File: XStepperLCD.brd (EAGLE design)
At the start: 49.5 x 38.1 mm, 43 parts, among them Q2 16 MHZ, U1 LCD-16X2NOHOLES

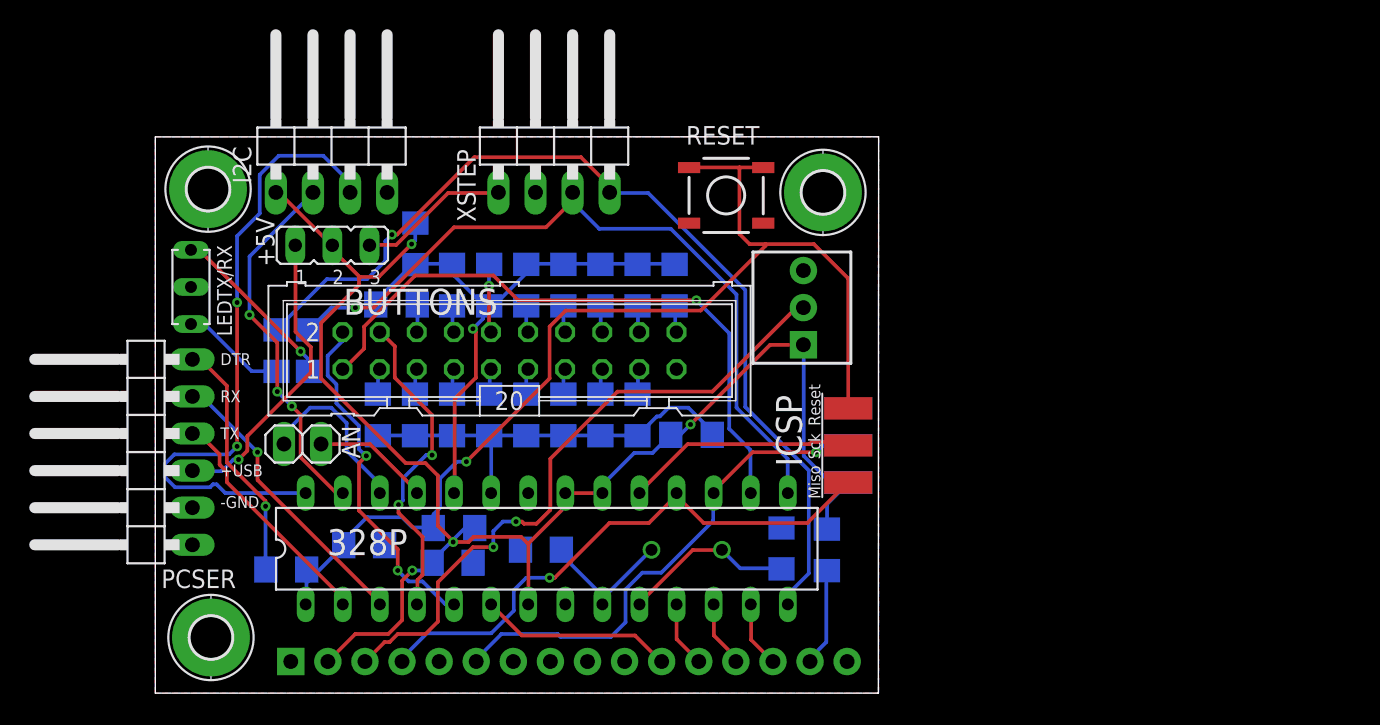
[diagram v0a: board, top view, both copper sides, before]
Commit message: - get button values only from A0
- stop/restart all threads in get values command
- refresh silkscreen in board and design
- set version 0.2 in code
- remove some comments
- add group init for threads
- reformat code
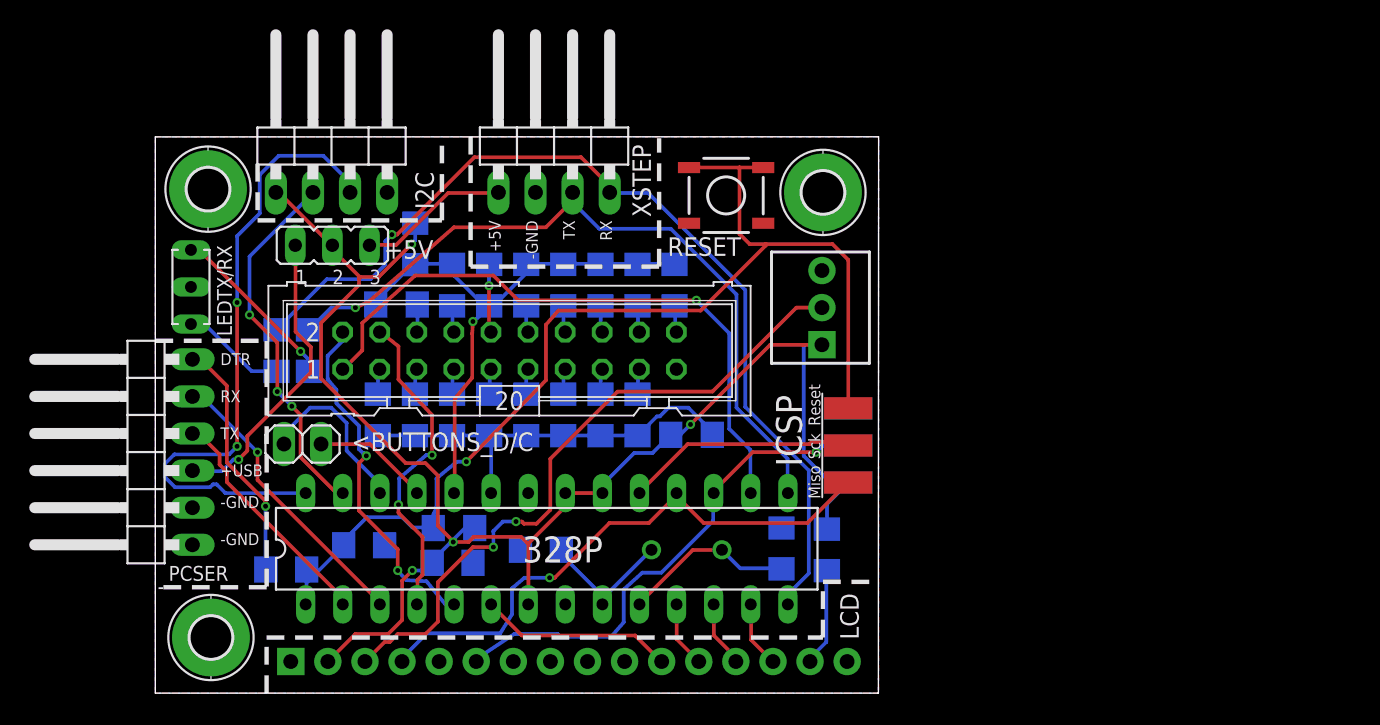
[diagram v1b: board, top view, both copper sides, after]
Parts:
- R2: value 220 -> 0-220R
- moved R1 1.27 mm to (45.3, 26.4)
- renumbered AN to <BUTTONS_D/C
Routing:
- net VCC: track 104.4 -> 106.9 mm
- net N$1: track 44.5 -> 45.7 mm
- net RESET: track 76.1 -> 77.1 mm
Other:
- board text added: "+5V"
- board text added: "680R"
- board text added: "LCD"
- board text added: "XLCD 0.2/092013"
- board text removed: "XSTEP 0.2 / 092013"

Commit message: - bugfic: set all buttons resistor to different values
- fix schema and board
- fix some typos and bugs in readButtons
- add thread to read buttons
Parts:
- R10, R18: value 680 -> 1.8k
- R11, R19: value 680 -> 2.2k
- R12, R20: value 680 -> 2.7k
- R13, R21: value 680 -> 3.3k
- R14, R22: value 680 -> 3.9k
- R15, R23: value 680 -> 4.7k
- R17, R9: value 680 -> 1.2k
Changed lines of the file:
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@@
 <?xml version="1.0" encoding="utf-8"?>
 <!DOCTYPE eagle SYSTEM "eagle.dtd">
-<eagle version="6.5.0">
+<eagle version="6.3">
 <drawing>
 <settings>
@@
 <wire x1="49.53" y1="38.1" x2="0" y2="38.09" width="0" layer="20"/>
 <wire x1="0" y1="38.09" x2="0" y2="0" width="0" layer="20"/>
-<dimension x1="0" y1="48.26" x2="49.53" y2="48.26" x3="24.765" y3="63.5" textsize="1.778" layer="51"/>
-<dimension x1="49.53" y1="48.26" x2="49.53" y2="0" x3="58.42" y3="24.13" textsize="1.778" layer="51"/>
+<dimension x1="0" y1="48.26" x2="49.53" y2="48.26" x3="24.765" y3="63.5" layer="51"/>
+<dimension x1="49.53" y1="48.26" x2="49.53" y2="0" x3="58.42" y3="24.13" layer="51"/>
 <text x="44.28" y="15.525" size="1.778" layer="25" rot="R90">ICSP</text>
 <text x="45.54" y="18.31" size="0.8128" layer="25" rot="R90">Reset</text>
@@
 </element>
 <element name="R8" library="resistor" package="R1206" value="680" x="16.515" y="26.61" smashed="yes" rot="MR0"/>
-<element name="R9" library="resistor" package="R1206" value="680" x="20.32" y="27.94" smashed="yes" rot="MR90"/>
-<element name="R10" library="resistor" package="R1206" value="680" x="22.86" y="27.94" smashed="yes" rot="MR270"/>
-<element name="R11" library="resistor" package="R1206" value="680" x="25.4" y="27.94" smashed="yes" rot="MR90"/>
-<element name="R12" library="resistor" package="R1206" value="680" x="27.94" y="27.94" smashed="yes" rot="MR90"/>
-<element name="R13" library="resistor" package="R1206" value="680" x="30.48" y="27.94" smashed="yes" rot="MR90"/>
-<element name="R14" library="resistor" package="R1206" value="680" x="33.02" y="27.94" smashed="yes" rot="MR90"/>
-<element name="R15" library="resistor" package="R1206" value="680" x="35.56" y="27.94" smashed="yes" rot="MR90"/>
+<element name="R9" library="resistor" package="R1206" value="1.2k" x="20.32" y="27.94" smashed="yes" rot="MR90"/>
+<element name="R10" library="resistor" package="R1206" value="1.8k" x="22.86" y="27.94" smashed="yes" rot="MR270"/>
+<element name="R11" library="resistor" package="R1206" value="2.2k" x="25.4" y="27.94" smashed="yes" rot="MR90"/>
+<element name="R12" library="resistor" package="R1206" value="2.7k" x="27.94" y="27.94" smashed="yes" rot="MR90"/>
+<element name="R13" library="resistor" package="R1206" value="3.3k" x="30.48" y="27.94" smashed="yes" rot="MR90"/>
+<element name="R14" library="resistor" package="R1206" value="3.9k" x="33.02" y="27.94" smashed="yes" rot="MR90"/>
+<element name="R15" library="resistor" package="R1206" value="4.7k" x="35.56" y="27.94" smashed="yes" rot="MR90"/>
 <element name="R16" library="resistor" package="R1206" value="680" x="33.02" y="19.05" smashed="yes" rot="MR270"/>
-<element name="R17" library="resistor" package="R1206" value="680" x="30.48" y="19.05" smashed="yes" rot="MR270"/>
-<element name="R18" library="resistor" package="R1206" value="680" x="27.94" y="19.05" smashed="yes" rot="MR270"/>
-<element name="R19" library="resistor" package="R1206" value="680" x="25.4" y="19.05" smashed="yes" rot="MR270"/>
-<element name="R20" library="resistor" package="R1206" value="680" x="22.86" y="19.05" smashed="yes" rot="MR270"/>
-<element name="R21" library="resistor" package="R1206" value="680" x="20.32" y="19.05" smashed="yes" rot="MR270"/>
-<element name="R22" library="resistor" package="R1206" value="680" x="17.78" y="19.05" smashed="yes" rot="MR270"/>
-<element name="R23" library="resistor" package="R1206" value="680" x="15.24" y="19.05" smashed="yes" rot="MR270"/>
+<element name="R17" library="resistor" package="R1206" value="1.2k" x="30.48" y="19.05" smashed="yes" rot="MR270"/>
+<element name="R18" library="resistor" package="R1206" value="1.8k" x="27.94" y="19.05" smashed="yes" rot="MR270"/>
+<element name="R19" library="resistor" package="R1206" value="2.2k" x="25.4" y="19.05" smashed="yes" rot="MR270"/>
+<element name="R20" library="resistor" package="R1206" value="2.7k" x="22.86" y="19.05" smashed="yes" rot="MR270"/>
+<element name="R21" library="resistor" package="R1206" value="3.3k" x="20.32" y="19.05" smashed="yes" rot="MR270"/>
+<element name="R22" library="resistor" package="R1206" value="3.9k" x="17.78" y="19.05" smashed="yes" rot="MR270"/>
+<element name="R23" library="resistor" package="R1206" value="4.7k" x="15.24" y="19.05" smashed="yes" rot="MR270"/>
 <element name="&lt;BUTTONS_D/C" library="pinhead" package="1X02" value="Analog" x="10.08" y="17.06" smashed="yes" rot="R180">
 <attribute name="NAME" x="13.4288" y="16.5788" size="1.27" layer="25" ratio="10"/>
@@
 </signal>
 </signals>
-<errors>
-</errors>
 </board>
 </drawing>

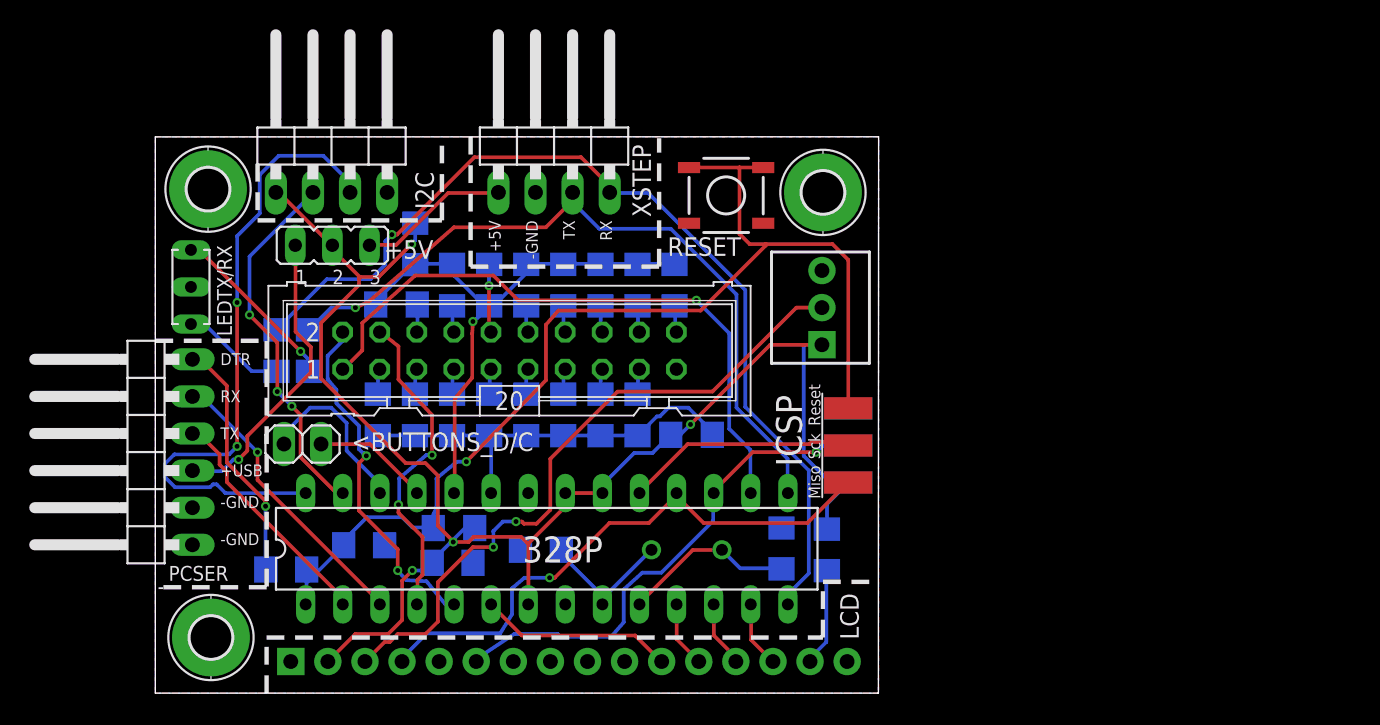
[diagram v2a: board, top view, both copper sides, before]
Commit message: - replace some TH parts with SMD and bugfixes
- remove reset button
- remove power pin and choose only power from xstepper
- add RJ45 plugin for connect XStepper
- change all button resistors to 680r and connect serial
- remove LED from serial line and put a new one to A7
- add some text to I2C
- change Atmega328 to SMD Version
- change Quartz to SMD ceramic resonator (16MHz)
- replace ICSP to normal 2x3 pin header
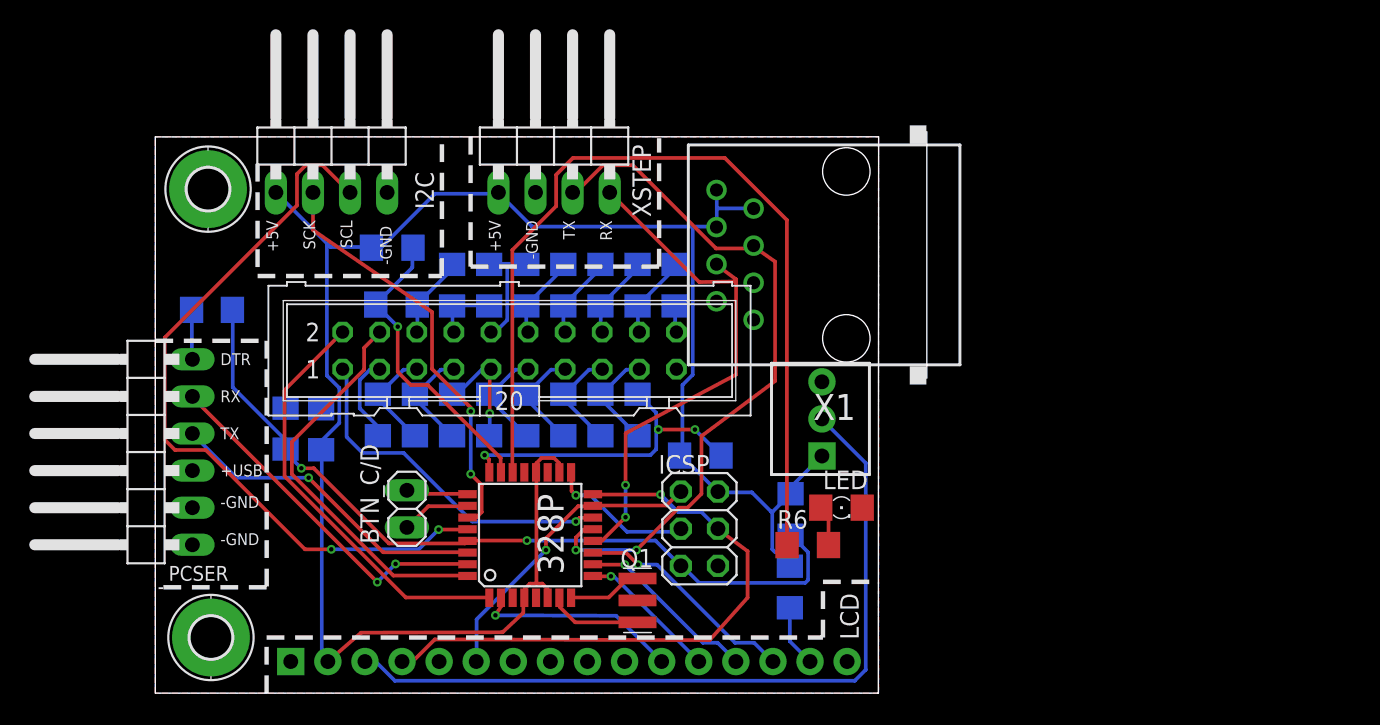
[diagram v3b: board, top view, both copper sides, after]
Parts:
- removed +5V: USB_VCC, jumper:JP2
- removed <BUTTONS_D/C: Analog, pinhead:1X02
- removed C14, C15: 18pF, resistor:C1206
- removed H6: MOUNT-PAD-ROUND2.8, holes:2,8-PAD
- removed LEDTX/RX: (no value), led:DUOLED2X5
- removed Q2: 16 MHZ, crystal:HC49/S
- removed R7: 110, resistor:R1206
- removed RESET: RESET, SparkFun:TACTILE_SWITCH_SMD
- added BTN_C/D: Analog, pinhead:1X02
- added LED: (no value), led:1206
- added Q1: (no value), murata-filter:CSTCR6M
- added X1: RJ45-6L-B, con-tycoelectronics:RJ45-NO-SHIELD
- 328P: device Bibsatmel:DIL28-3 -> atmel:TQFP32-08
- ICSP: value ICSP -> (none); device avr-7:6PAD_ISP -> pinhead:2X03
- R10, R18: value 1.8k -> 680
- R11, R19: value 2.2k -> 680
- R12, R20: value 2.7k -> 680
- R13, R21: value 3.3k -> 680
- R14, R22: value 3.9k -> 680
- R15, R23: value 4.7k -> 680
- R17, R9: value 1.2k -> 680
- R6: value 110 -> 160R
- moved R6 38.7 mm to (44.7, 10.1), flipped to the top, turned to 0 degrees
- moved R3 23.1 mm to (43.5, 12.2), turned to 90 degrees
- moved C1 18.5 mm to (3.88, 26.2)
- moved C12 12.8 mm to (11.4, 18.1), turned to 270 degrees
- moved ICSP 11.7 mm to (37.3, 11.3), turned to 270 degrees
- moved C13 9.62 mm to (8.92, 18.1), turned to 270 degrees
- moved R1 7.62 mm to (45.3, 18.8)
- moved R2 3.59 mm to (43.5, 7.27)
- moved R5 1.60 mm to (16.2, 30.5), turned to 0 degrees
- moved R4 1.54 mm to (37.3, 16.3)
- moved 328P 1.47 mm to (25.7, 10.8), turned to 90 degrees
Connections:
- removed net N$12 (its old number): BUTTONS.12, R11.1
- removed net N$16: BUTTONS.7, R21.1
- removed net N$17: BUTTONS.9, R20.1
- removed net N$18: BUTTONS.11, R19.1
- removed net N$19: BUTTONS.18, R14.1
- removed net N$21: LEDTX/RX.AG, R6.2
- removed net N$22: LEDTX/RX.AR, R7.1
- removed net N$33: 328P.9, C15.1, Q2.1
- removed net USB_5V: +5V.1, PCSER.3
- removed net XSTEP_5V: +5V.3, XSTEP.1
- new net N$23: BUTTONS.17, R16.2, R17.1
- new net N$24: BUTTONS.15, R17.2, R18.1
- new net N$25: BUTTONS.13, R18.2, R19.1
- new net N$26: BUTTONS.11, R19.2, R20.1
- new net N$27: BUTTONS.9, R20.2, R21.1
- new net N$28: BUTTONS.7, R21.2, R22.1
- new net N$29: BUTTONS.5, R22.2, R23.1
- new net N$3: 328P.7, Q1.1
- net BUTTONS_A: now also R5.1, R8.2; no longer R16.2, R17.2, R18.2, R19.2, R20.2, R21.2, R22.2, R23.2, R4.1
- net BUTTONS_B: now also R16.1, R4.1; no longer R10.2, R11.2, R12.2, R13.2, R14.2, R15.2, R5.1, R8.2, R9.2
- net BUTTONS_C: now also BTN_C/D.1; no longer <BUTTONS_D/C.1
- net BUTTONS_D: now also BTN_C/D.2; no longer <BUTTONS_D/C.2
- net D4: now also 328P.2; no longer 328P.6
- net D5: now also 328P.9; no longer 328P.11
- net D6: now also 328P.10; no longer 328P.12
- net D7: now also 328P.11; no longer 328P.13
- net ENABLE/MOSI: now also 328P.15, ICSP.1; no longer 328P.17, ICSP.MOSI
- net GND: now also 328P.21, 328P.3, 328P.5, ICSP.6, LED.C, Q1.2, X1.1, X1.2, X1.3; no longer 328P.22, 328P.8, C14.2, C15.2, H6.B2,8, ICSP.GND, LEDTX/RX.K, RESET.1, RESET.2
- net N$10: now also BUTTONS.18, R14.1, R15.2; no longer BUTTONS.5, R22.1
- net N$11: now also BUTTONS.14, R12.1, R13.2; no longer BUTTONS.10, R10.1
- net N$13: now also LED.A, R6.2; no longer BUTTONS.14, R12.1
- net N$15: now also 328P.22, R6.1; no longer BUTTONS.16, R13.1
- net N$34: now also 328P.8, Q1.3; no longer 328P.10, C14.1, Q2.2
- net N$4: now also BUTTONS.3, R23.2; no longer BUTTONS.13, R18.1
- net N$5: now also BUTTONS.6, R8.1, R9.2; no longer BUTTONS.15, R17.1
- net N$6: now also BUTTONS.8, R10.2, R9.1; no longer BUTTONS.17, R16.1
- net N$7: now also BUTTONS.10, R10.1, R11.2; no longer BUTTONS.6, R8.1
- net N$8: now also BUTTONS.12, R11.1, R12.2; no longer BUTTONS.8, R9.1
- net N$9: now also BUTTONS.16, R13.1, R14.2; no longer BUTTONS.3, R23.1
- net POT_A: now also 328P.32; no longer 328P.4
- net POT_B: now also 328P.1; no longer 328P.5
- net POT_SELECT: now also 328P.14; no longer 328P.16
- net RESET: now also 328P.29, ICSP.5; no longer 328P.1, ICSP.RST, RESET.3, RESET.4
- net RS/MISO: now also 328P.16, ICSP.4; no longer 328P.18, ICSP.MISO
- net RX: now also 328P.12, X1.4; no longer 328P.14, R6.1
- net SCK: now also 328P.17, ICSP.3; no longer 328P.19, ICSP.SCK
- net TX: now also 328P.13, X1.5; no longer 328P.15, R7.2
- net USB_RXD: now also 328P.31; no longer 328P.3
- net USB_TXD: now also 328P.30; no longer 328P.2
- net VCC: now also 328P.18, 328P.4, 328P.6, ICSP.2, X1.6, X1.7, X1.8, XSTEP.1; no longer +5V.2, 328P.21, 328P.7, ICSP.VCC
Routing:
- net N$15: track 1.84 -> 61.9 mm
- net RX: track 65.9 -> 36.7 mm, vias 1 -> 2
- net VCC: track 106.9 -> 132.2 mm, vias 4 -> 0
- net RESET: track 77.1 -> 54.5 mm, vias 1 -> 2
- net USB_5V: track 20.7 -> 0.00 mm, vias 1 -> 0
- net POT_SELECT: track 43.4 -> 24.1 mm
- net BUTTONS_B: track 39.7 -> 22.7 mm, vias 1 -> 3
- net N$14: track 16.8 -> 3.40 mm, vias 1 -> 0
- net ENABLE/MOSI: track 34.2 -> 21.0 mm
- net N$22: track 12.0 -> 0.00 mm, vias 1 -> 0
- net D7: track 4.55 -> 15.4 mm, vias 0 -> 1
- net XSTEP_5V: track 10.3 -> 0.00 mm
- net N$33: track 10.0 -> 0.00 mm
- net BUTTONS_A: track 28.7 -> 20.7 mm, vias 0 -> 1
- net D6: track 4.54 -> 12.6 mm, vias 0 -> 1
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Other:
- board text added: "SCK"
- board text added: "SCL"
- board text added: "XLCD 0.3/012014"
- board text removed: "ICSP"
- board text removed: "Miso"
- board text removed: "Reset"
- board text removed: "Sck"
- board text removed: "XLCD 0.2/092013"

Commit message: make board bigger
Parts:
- added H1, H2: MOUNT-PAD-ROUND2.8, holes:2,8-PAD
- moved XSTEP 35.6 mm to (62.9, 36.8)
- moved R1 32.2 mm to (15.0, 8.00), turned to 0 degrees
- moved X1 29.0 mm to (74.0, 18.6)
- moved R3 22.9 mm to (20.6, 13.5)
- moved R4 17.7 mm to (53.8, 22.6)
- moved R16 17.3 mm to (49.5, 24.1)
- moved R17 17.3 mm to (47.0, 24.1)
- moved R18 17.3 mm to (44.5, 24.1)
- moved R19 17.3 mm to (41.9, 24.1)
- moved R20 17.3 mm to (39.4, 24.1)
- moved R21 17.3 mm to (36.8, 24.1)
- moved R22 17.3 mm to (34.3, 24.1)
- moved R23 17.3 mm to (31.8, 24.1)
- moved R8 16.5 mm to (31.7, 33.0), turned to 90 degrees
- moved BUTTONS 14.9 mm to (38.2, 28.5)
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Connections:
- net BUTTONS_C: now also 328P.19; no longer 328P.25
- net BUTTONS_D: now also 328P.22; no longer 328P.26
- net ENABLE/MOSI: now also ICSP.4; no longer ICSP.1
- net N$15: now also 328P.25; no longer 328P.22
- net RS/MISO: now also ICSP.1; no longer ICSP.4
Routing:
- net N$15: track 61.9 -> 6.72 mm, vias 0 -> 2
- net N$1: track 53.6 -> 5.78 mm
- net SCL: track 51.0 -> 26.0 mm
- net VCC: track 132.2 -> 156.9 mm, vias 0 -> 4
- net RX: track 36.7 -> 54.4 mm, vias 2 -> 0
- net POT_SELECT: track 24.1 -> 41.4 mm, vias 1 -> 2
- net RESET: track 54.5 -> 37.5 mm
- net BUTTONS_C: track 4.26 -> 19.0 mm, vias 0 -> 2
- net BUTTONS_D: track 4.76 -> 18.7 mm, vias 0 -> 2
- net USB_RXD: track 24.7 -> 38.6 mm, vias 2 -> 4
- net USB_TXD: track 22.2 -> 34.0 mm, vias 1 -> 4
- net SCK: track 10.0 -> 20.6 mm
- net ENABLE/MOSI: track 21.0 -> 30.6 mm, vias 1 -> 3
- net TX: track 48.3 -> 57.6 mm
- net POT_B: track 29.0 -> 20.9 mm, vias 0 -> 2
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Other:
- board size 49.5 x 38.1 mm -> 78.7 x 38.1 mm
- board text added: "GND"
- board text added: "SDA"
- board text removed: "SCK"
